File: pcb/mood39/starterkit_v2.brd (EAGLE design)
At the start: 32 x 32 mm, 17 parts, among them IC1 TINY85, IC2 LM2940, X1 PWRUSB, X3 PWRUNREG

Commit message: start routing
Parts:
- C3: device rcl:C025-025X050 -> rcl:C0805
- moved R3 5.43 mm to (22.2, 11.4), turned to 90 degrees
- moved X3 2.62 mm to (10.8, 4.45)
- moved R6 2.29 mm to (25.4, 10.8)
- moved C3 2.22 mm to (20.0, 2.54), flipped to the bottom
- moved R2 1.35 mm to (6.99, 25.7)
- moved SV1 0.95 mm to (12.7, 27.3)
- moved C1 0.71 mm to (3.81, 24.1)
- moved R4 0.63 mm to (22.2, 15.9)
- moved IC2 0.32 mm to (21.9, 6.03)
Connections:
- net N$2 renamed V+
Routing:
- net VCC: track 0.00 -> 70.3 mm
- net MISO: track 0.00 -> 40.7 mm, vias 0 -> 2
- net MOSI: track 0.00 -> 40.4 mm, vias 0 -> 2
- net _RESET: track 0.00 -> 30.7 mm
- net PB3: track 0.00 -> 19.6 mm
- net V+: track 0.00 -> 19.1 mm
- net SCK: track 0.00 -> 19.1 mm
- net N$5: track 0.00 -> 14.2 mm
- net N$6: track 0.00 -> 10.0 mm
- net PB4: track 0.00 -> 7.27 mm
- net N$7: track 0.00 -> 4.46 mm
- net N$1: track 0.00 -> 3.20 mm

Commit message: commit before battery low
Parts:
- moved C1 1.31 mm to (5.08, 23.8)
- moved C2 0.45 mm to (29.2, 6.67)
- moved LED2 0.45 mm to (29.2, 11.4)
- moved R2 0.45 mm to (7.30, 26.0)
- moved R4 0.32 mm to (22.2, 15.6)
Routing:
- net SCK: track 19.1 -> 52.0 mm, vias 0 -> 2
- net VCC: track 70.3 -> 58.7 mm
- net MOSI: track 40.4 -> 44.6 mm
- net PB3: track 19.6 -> 16.7 mm
- net MISO: track 40.7 -> 42.1 mm

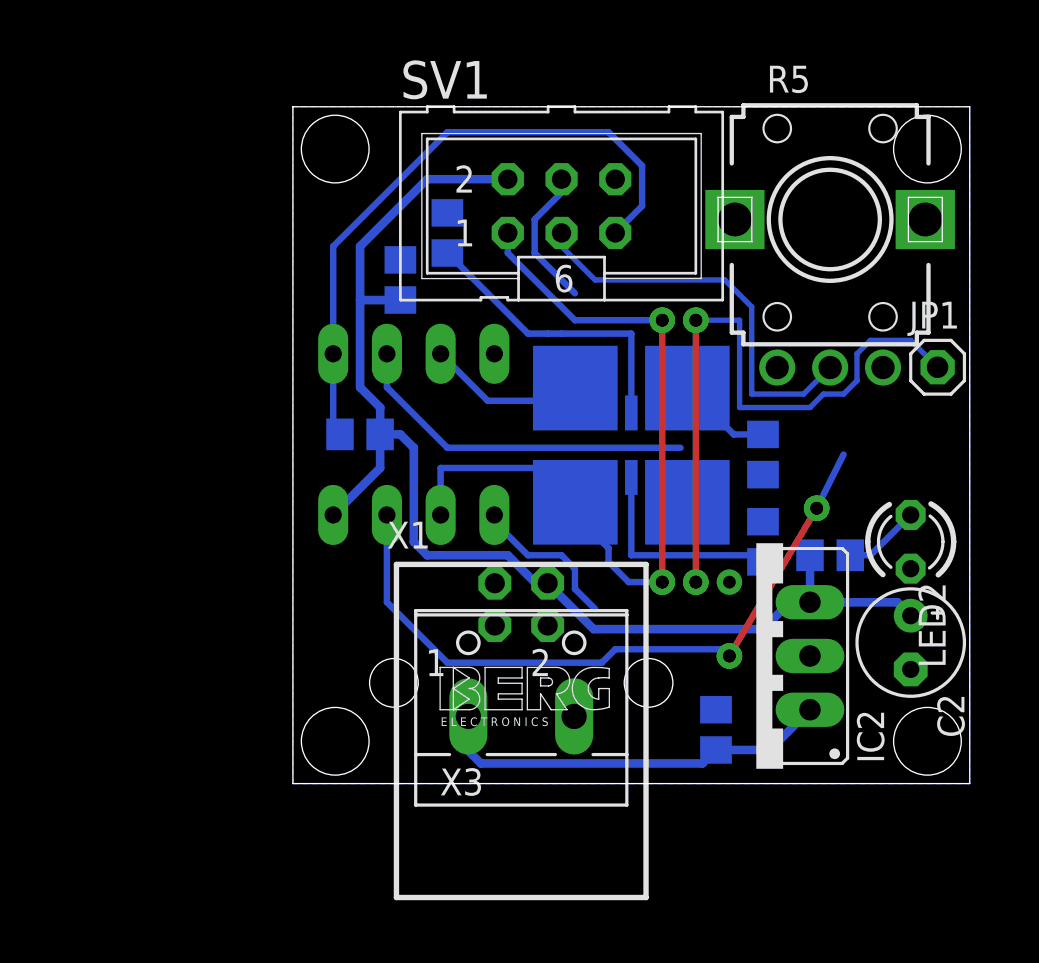
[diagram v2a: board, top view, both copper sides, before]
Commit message: routing to a point where the right packages are needed
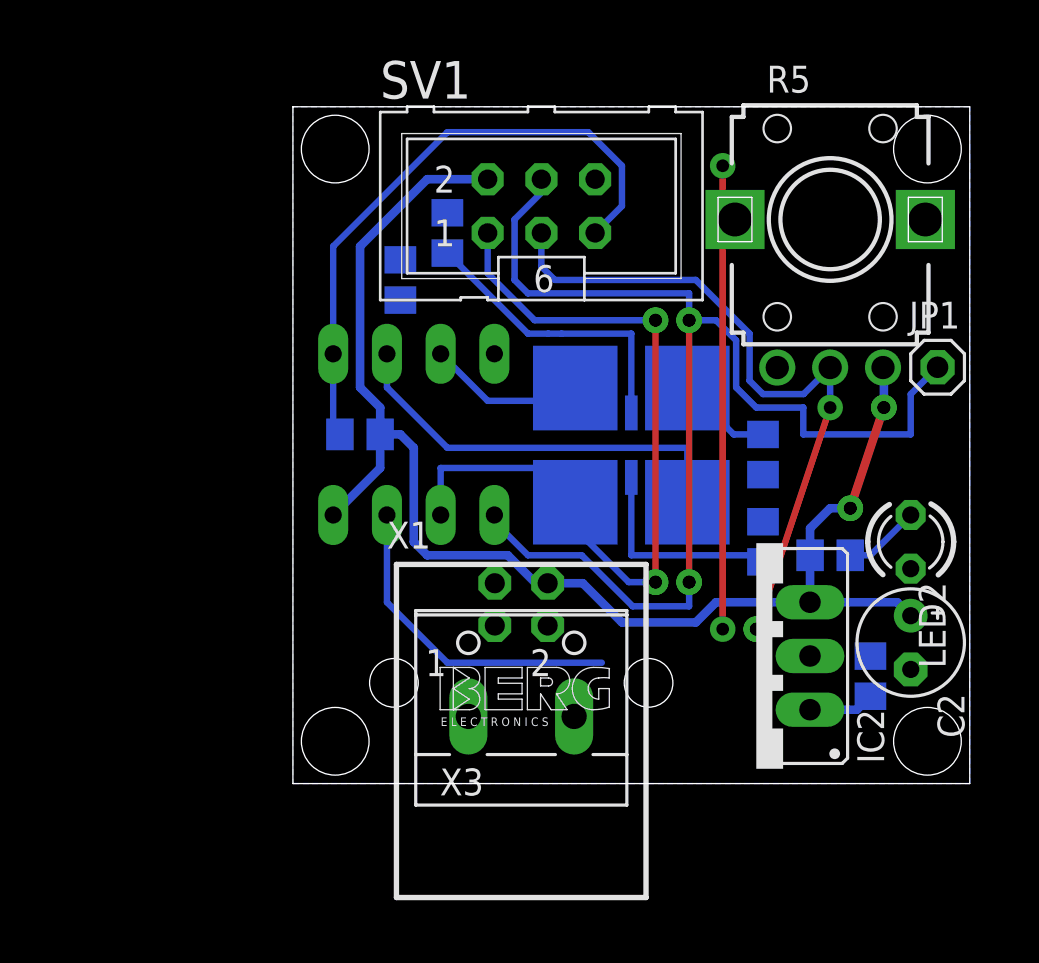
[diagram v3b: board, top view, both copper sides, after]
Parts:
- LED2: value (none) -> rot lc
- R6: value (none) -> 1.5k
- moved C3 7.73 mm to (27.3, 5.08)
- moved SV1 0.95 mm to (11.7, 27.3)
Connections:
- net GND: now also X3.1; no longer X3.2
- net V+: now also X3.2; no longer X3.1
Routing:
- net GND1: track 0.00 -> 21.9 mm, vias 0 -> 2
- net V+: track 19.1 -> 3.12 mm
- net MOSI: track 44.6 -> 58.2 mm
- net VCC: track 58.7 -> 66.1 mm, vias 0 -> 2
- net SCK: track 52.0 -> 48.0 mm
- net PB3: track 16.7 -> 19.6 mm
- net MISO: track 42.1 -> 43.6 mm
- net _RESET: track 30.2 -> 29.3 mm

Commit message: der miniaturtaster ist arg groß
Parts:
- added S1: (no value), switch-omron:B3F-10XX
- moved LED2 27.1 mm to (2.22, 8.89)
- moved R6 10.8 mm to (19.7, 1.59), turned to 0 degrees
- moved C3 7.05 mm to (20.3, 4.13), turned to 180 degrees
- moved IC2 6.30 mm to (26.7, 10.2), turned to 0 degrees
- moved C2 5.39 mm to (25.4, 2.86), turned to 180 degrees
- moved R4 5.02 mm to (27.0, 14.0)
- moved R3 1.59 mm to (23.2, 12.7), turned to 180 degrees
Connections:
- net GND: now also S1.3, S1.4
- net MOSI: now also S1.1, S1.2
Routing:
- net MOSI: track 58.2 -> 0.00 mm, vias 2 -> 0
- net VCC: track 66.1 -> 34.8 mm, vias 2 -> 0
- net SCK: track 48.0 -> 35.0 mm, vias 2 -> 0
- net N$7: track 4.48 -> 9.45 mm
- net N$1: track 3.65 -> 0.00 mm
- net V+: track 3.12 -> 0.00 mm
- net N$6: track 10.0 -> 11.1 mm

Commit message: teile ersetzt durch tatsächlich verfügbare
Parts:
- removed X3: PWRUNREG, con-wago-500:W237-102
- added U$1: RIACON_101_2, n39:RIACON_101_2
- R5: value EVUF2A -> ALPS_RK09K113; device pot:EVUF -> n39:ALPS_RK09K113
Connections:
- new net !RESET: IC1.1, R1.2
- net GND: now also R5.3, U$1.1; no longer R5.1, X3.1
- net V+: now also U$1.2; no longer X3.2
- net VCC: now also R5.1; no longer R5.3
- net _RESET: no longer IC1.1, R1.2
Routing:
- net _RESET: track 29.3 -> 20.2 mm
- net !RESET: track 0.00 -> 3.94 mm
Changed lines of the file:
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@@
 <layer number="44" name="Drills" color="7" fill="1" visible="no" active="yes"/>
 <layer number="45" name="Holes" color="7" fill="1" visible="yes" active="yes"/>
-<layer number="46" name="Milling" color="3" fill="1" visible="no" active="yes"/>
+<layer number="46" name="Milling" color="3" fill="1" visible="yes" active="yes"/>
 <layer number="47" name="Measures" color="7" fill="1" visible="no" active="yes"/>
 <layer number="48" name="Document" color="7" fill="1" visible="yes" active="yes"/>
@@
 </element>
 <element name="IC2" library="v-reg" package="78XXS" value="LM2940" x="26.67" y="10.16"/>
-<element name="X3" library="con-wago-500" package="W237-102" value="PWRUNREG" x="10.795" y="4.445">
-<attribute name="OC_NEWARK" value="70K9898" x="28.575" y="-36.195" size="1.778" layer="27" display="off"/>
-<attribute name="MPN" value="237-102" x="28.575" y="-36.195" size="1.778" layer="27" display="off"/>
-<attribute name="MF" value="" x="28.575" y="-36.195" size="1.778" layer="27" display="off"/>
-<attribute name="OC_FARNELL" value="unknown" x="28.575" y="-36.195" size="1.778" layer="27" display="off"/>
-</element>
 <element name="C2" library="rcl" package="E2,5-5" value="47u" x="25.4" y="2.8575" rot="R180"/>
 <element name="C3" library="rcl" package="C0805" value="470n" x="20.32" y="4.1275" rot="MR180"/>
-<element name="R5" library="pot" package="EVUF" value="EVUF2A" x="25.4" y="26.67"/>
+<element name="R5" library="n39" package="ALPS_RK09K113" value="ALPS_RK09K113" x="25.4" y="26.67"/>
 <element name="JP1" library="pinhead" package="1X01" value="I2CDAT" x="30.48" y="19.685"/>
 <element name="LED2" library="led" package="LED3MM" value="rot lc" x="2.2225" y="8.89" rot="R270"/>
@@
 <attribute name="MF" value="" x="22.5425" y="3.81" size="1.778" layer="27" display="off"/>
 <attribute name="OC_FARNELL" value="176432" x="22.5425" y="3.81" size="1.778" layer="27" display="off"/>
+</element>
+<element name="U$1" library="n39" package="RIACON_101_2" value="RIACON_101_2" x="-6.6675" y="0.9525">
+<attribute name="REICHELT" value="AKL 101-02" x="-6.6675" y="0.9525" size="1.778" layer="27" display="off"/>
 </element>
 </elements>
@@
 <vertex x="0" y="32"/>
 </polygon>
-<contactref element="R5" pad="1"/>
+<contactref element="R5" pad="3"/>
 <contactref element="LED2" pad="K"/>
-<contactref element="X3" pad="1"/>
 <contactref element="S1" pad="3"/>
 <contactref element="S1" pad="4"/>
+<contactref element="U$1" pad="1"/>
 <wire x1="7.3025" y1="26.985" x2="14.2875" y2="28.575" width="0" layer="19" extent="16-16"/>
 <wire x1="5.08" y1="24.7625" x2="7.3025" y2="26.985" width="0" layer="19" extent="16-16"/>
 <wire x1="9.525" y1="20.32" x2="5.08" y2="24.7625" width="0" layer="19" extent="16-16"/>
-<wire x1="22.9" y1="19.67" x2="14.2875" y2="28.575" width="0" layer="19" extent="1-1"/>
-<wire x1="26.9875" y1="13.02" x2="22.9" y2="19.67" width="0" layer="19" extent="16-16"/>
-<wire x1="24.1275" y1="12.7" x2="26.9875" y2="13.02" width="0" layer="19" extent="16-16"/>
-<wire x1="26.67" y1="7.62" x2="24.1275" y2="12.7" width="0" layer="19" extent="16-16"/>
-<wire x1="21.27" y1="4.1275" x2="26.67" y2="7.62" width="0" layer="19" extent="16-16"/>
-<wire x1="24.13" y1="2.8575" x2="21.27" y2="4.1275" width="0" layer="19" extent="16-16"/>
-<wire x1="12.045" y1="7.4725" x2="24.1275" y2="12.7" width="0" layer="19" extent="16-16"/>
-<wire x1="8.295" y1="3.175" x2="12.045" y2="7.4725" width="0" layer="19" extent="1-1"/>
-<wire x1="2.2225" y1="7.62" x2="8.295" y2="3.175" width="0" layer="19" extent="1-1"/>
-<wire x1="25.7937" y1="1.5494" x2="2.2225" y2="7.62" width="0" layer="19" extent="1-1"/>
-<wire x1="19.2913" y1="1.5494" x2="25.7937" y2="1.5494" width="0" layer="19" extent="1-1"/>
+<wire x1="27.9" y1="19.67" x2="14.2875" y2="28.575" width="0" layer="19" extent="1-1"/>
+<wire x1="24.1275" y1="12.7" x2="27.9" y2="19.67" width="0" layer="19" extent="16-16"/>
+<wire x1="26.9875" y1="13.02" x2="24.1275" y2="12.7" width="0" layer="19" extent="16-16"/>
+<wire x1="26.67" y1="7.62" x2="26.9875" y2="13.02" width="0" layer="19" extent="16-16"/>
+<wire x1="24.13" y1="2.8575" x2="26.67" y2="7.62" width="0" layer="19" extent="1-1"/>
+<wire x1="25.7937" y1="1.5494" x2="24.13" y2="2.8575" width="0" layer="19" extent="1-1"/>
+<wire x1="21.27" y1="4.1275" x2="24.13" y2="2.8575" width="0" layer="19" extent="16-16"/>
+<wire x1="19.2913" y1="1.5494" x2="21.27" y2="4.1275" width="0" layer="19" extent="16-16"/>
+<wire x1="12.045" y1="7.4725" x2="19.2913" y2="1.5494" width="0" layer="19" extent="1-1"/>
+<wire x1="2.2225" y1="7.62" x2="12.045" y2="7.4725" width="0" layer="19" extent="1-1"/>
+<wire x1="-9.2075" y1="0.9525" x2="2.2225" y2="7.62" width="0" layer="19" extent="1-1"/>
 </signal>
 <signal name="VCC" class="1">
@@
 <contactref element="SV1" pad="2"/>
 <contactref element="X1" pad="1"/>
-<contactref element="R5" pad="3"/>
+<contactref element="R5" pad="1"/>
 <contactref element="R1" pad="1"/>
 <contactref element="R6" pad="1"/>
@@
 <wire x1="3.175" y1="25.4" x2="6.35" y2="28.575" width="0.4064" layer="16"/>
 <wire x1="6.35" y1="28.575" x2="9.2075" y2="28.575" width="0.4064" layer="16"/>
-<wire x1="29.21" y1="7.62" x2="27.9" y2="19.67" width="0" layer="19" extent="1-1"/>
+<wire x1="29.21" y1="7.62" x2="22.9" y2="19.67" width="0" layer="19" extent="1-1"/>
 <wire x1="26.67" y1="2.8575" x2="29.21" y2="7.62" width="0" layer="19" extent="1-1"/>
 <wire x1="20.635" y1="1.5875" x2="26.67" y2="2.8575" width="0" layer="19" extent="16-16"/>
@@
 <signal name="_RESET" class="2">
 <contactref element="SV1" pad="5"/>
-<contactref element="R1" pad="2"/>
-<contactref element="IC1" pad="1"/>
-<wire x1="1.905" y1="20.32" x2="1.905" y2="16.83" width="0.3048" layer="16"/>
-<wire x1="1.905" y1="16.83" x2="2.225" y2="16.51" width="0.3048" layer="16"/>
-<wire x1="1.905" y1="20.32" x2="1.905" y2="25.4" width="0.3048" layer="16"/>
 <wire x1="1.905" y1="25.4" x2="7.3025" y2="30.7975" width="0.3048" layer="16"/>
 <wire x1="14.2875" y1="26.035" x2="15.5575" y2="27.305" width="0.3048" layer="16"/>
@@
 <contactref element="IC2" pad="IN"/>
 <contactref element="C3" pad="1"/>
-<contactref element="X3" pad="2"/>
+<contactref element="U$1" pad="2"/>
 <wire x1="19.37" y1="4.1275" x2="24.13" y2="7.62" width="0" layer="19" extent="16-16"/>
-<wire x1="13.295" y1="3.175" x2="24.13" y2="7.62" width="0" layer="19" extent="1-1"/>
+<wire x1="-4.1275" y1="0.9525" x2="19.37" y2="4.1275" width="0" layer="19" extent="16-16"/>
 </signal>
 <signal name="N$1" class="2">
@@
 <signal name="N$11">
 </signal>
+<signal name="!RESET" class="2">
+<contactref element="R1" pad="2"/>
+<contactref element="IC1" pad="1"/>
+<wire x1="1.905" y1="20.32" x2="1.905" y2="16.83" width="0.3048" layer="16"/>
+<wire x1="1.905" y1="16.83" x2="2.225" y2="16.51" width="0.3048" layer="16"/>
+</signal>
 </signals>

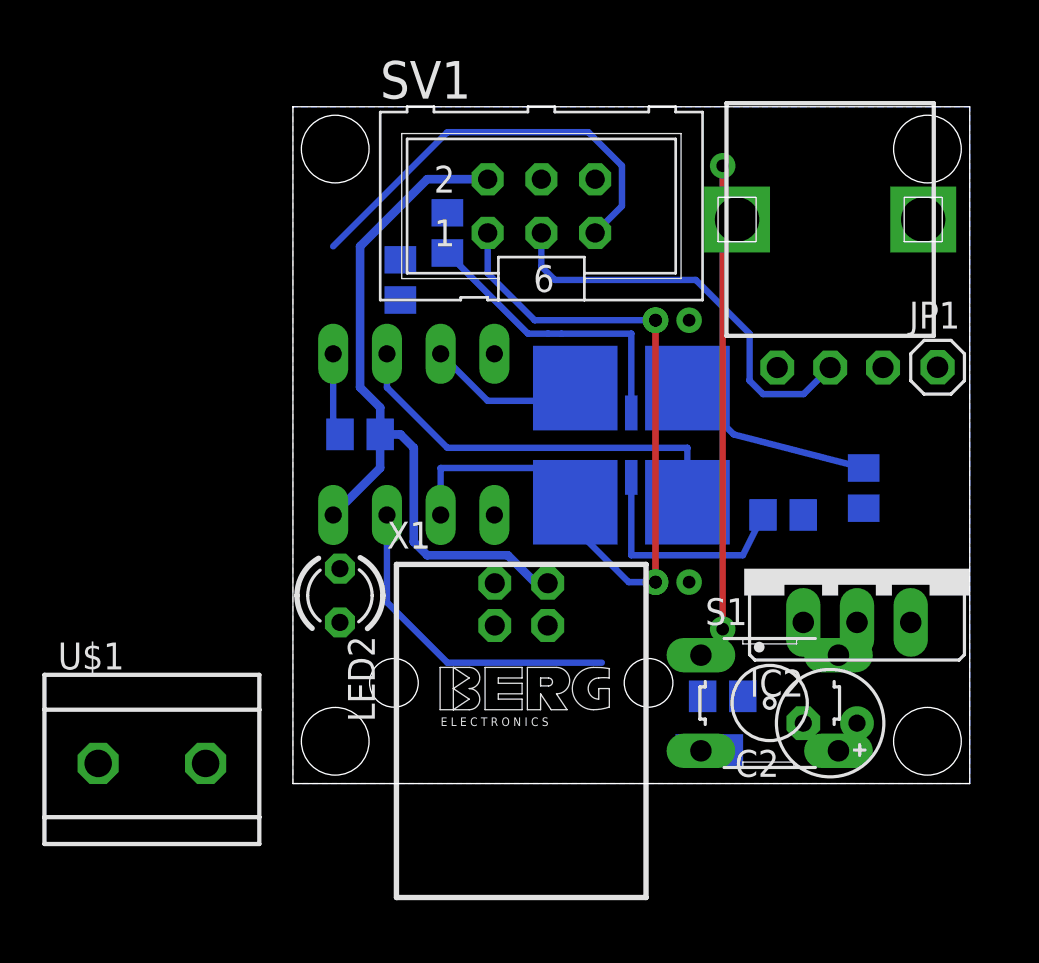
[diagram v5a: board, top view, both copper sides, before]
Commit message: Taster ersetzt
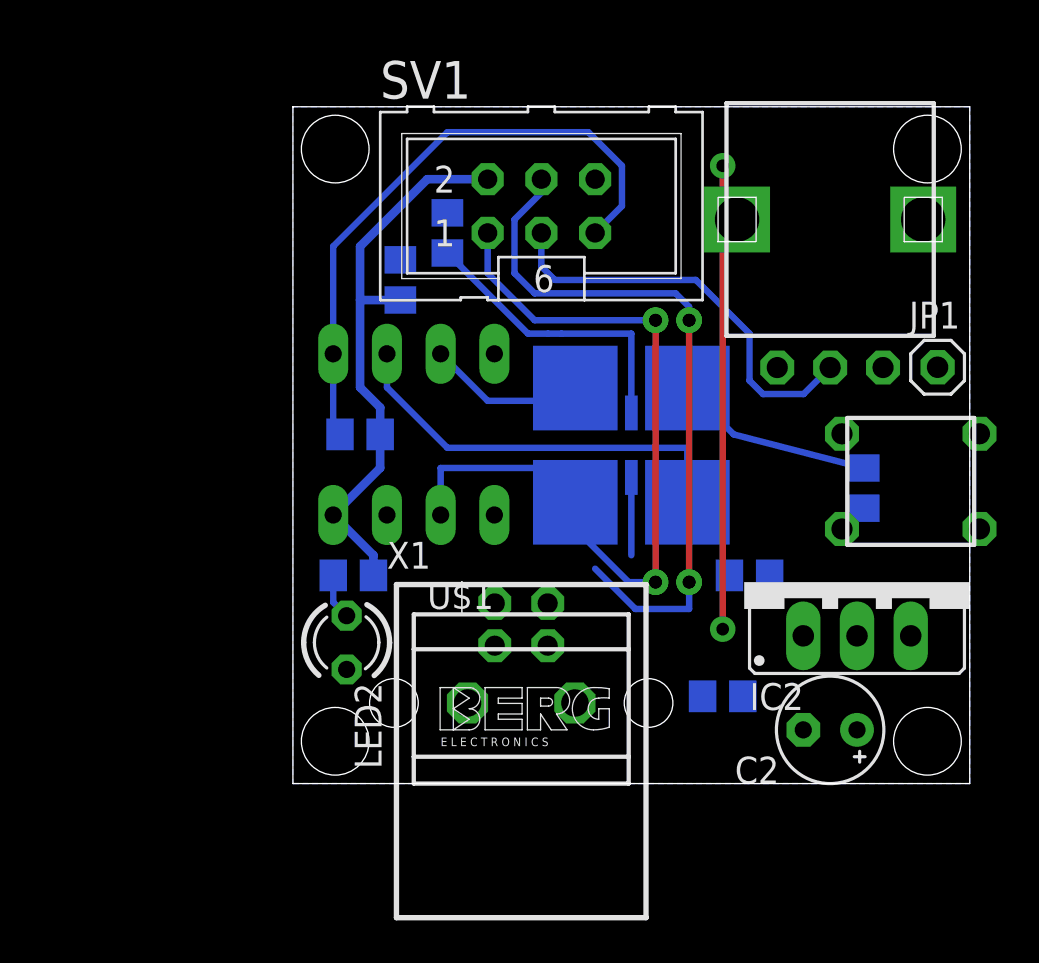
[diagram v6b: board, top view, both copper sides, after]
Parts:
- S1: device switch-omron:B3F-10XX -> n39:JTP-1130
- moved R6 18.7 mm to (2.86, 9.84)
- moved U$1 17.7 mm to (10.8, 3.81)
- moved S1 12.4 mm to (29.2, 14.3)
- moved R3 3.27 mm to (21.6, 9.84)
- moved LED2 2.25 mm to (2.54, 6.67)
- moved X1 0.95 mm to (10.8, 3.81)
- moved IC2 0.63 mm to (26.7, 9.53)
- moved C2 0.32 mm to (25.4, 2.54)
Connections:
- removed net _RESET: SV1.5
- net !RESET: now also SV1.5
- net GND: now also S1.1, S1.2; no longer S1.3, S1.4
- net MOSI: now also S1.3, S1.4; no longer S1.1, S1.2
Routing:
- net MOSI: track 0.00 -> 33.4 mm, vias 0 -> 2
- net !RESET: track 3.94 -> 29.3 mm
- net _RESET: track 20.2 -> 0.00 mm
- net SCK: track 35.0 -> 19.6 mm
- net VCC: track 34.8 -> 26.9 mm
- net N$6: track 11.1 -> 3.68 mm
- net N$1: track 0.00 -> 2.17 mm
